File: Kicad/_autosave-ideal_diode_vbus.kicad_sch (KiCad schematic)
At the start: 20 parts, among them J2 USB_B_Micro, Q3 AON7422G, Q4 AON7422G, U5 LD1117S33TR_SOT223, U6 LM74700QDBVRQ1, U7 LM74700QDBVTQ1

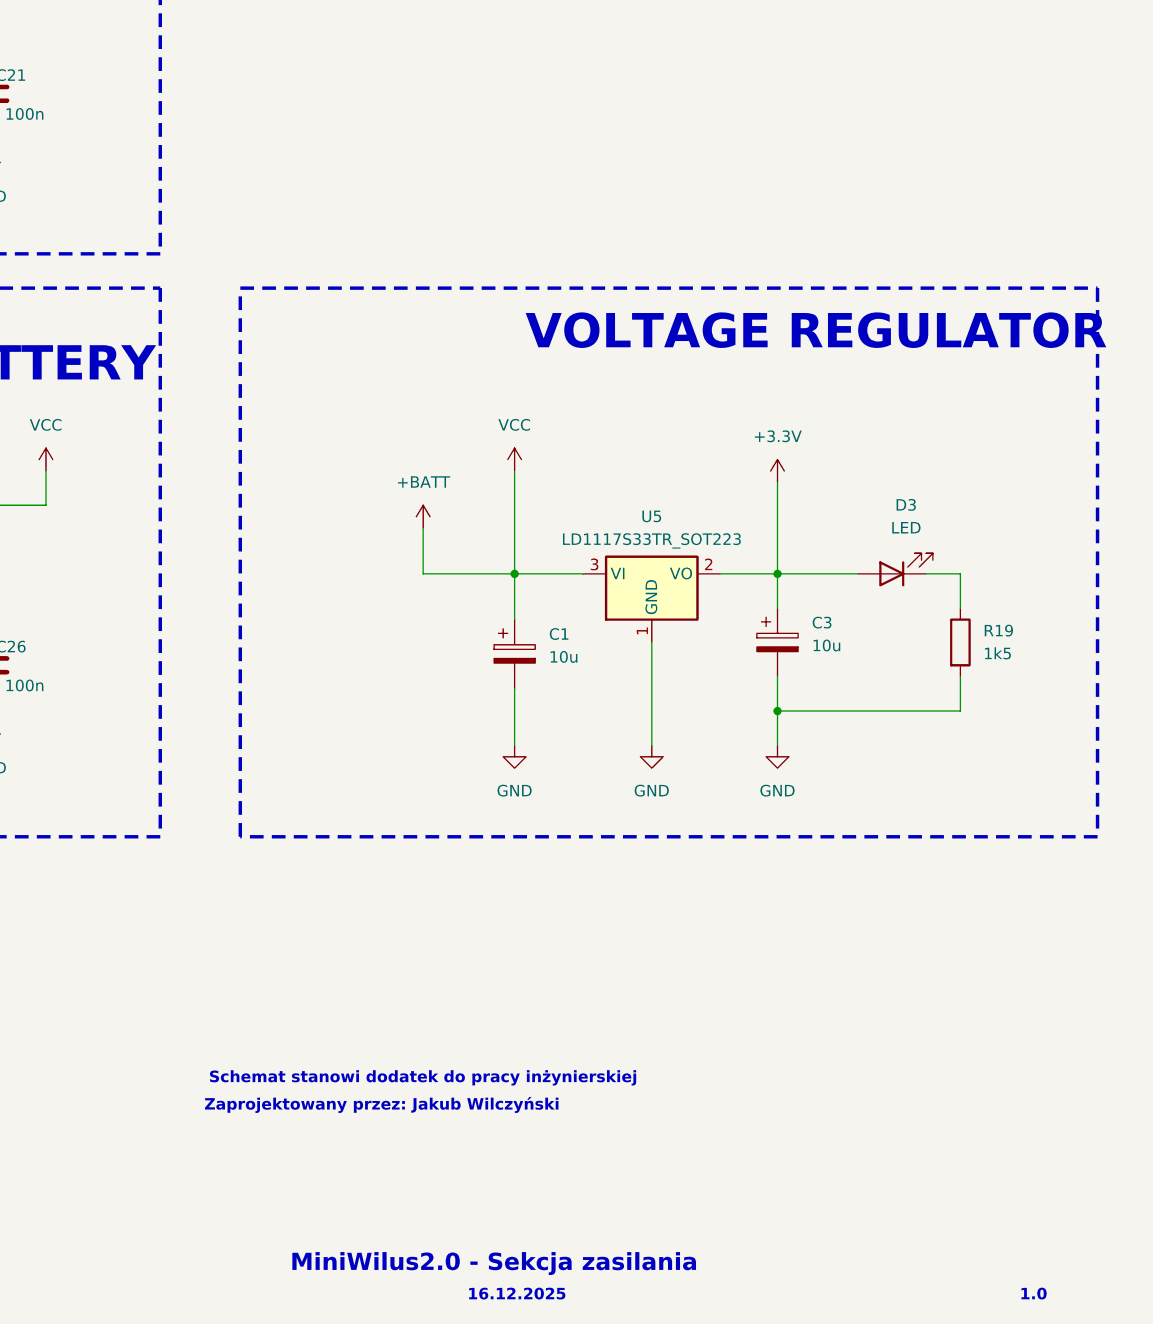
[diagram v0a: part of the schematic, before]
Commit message: kicad schemas documentation
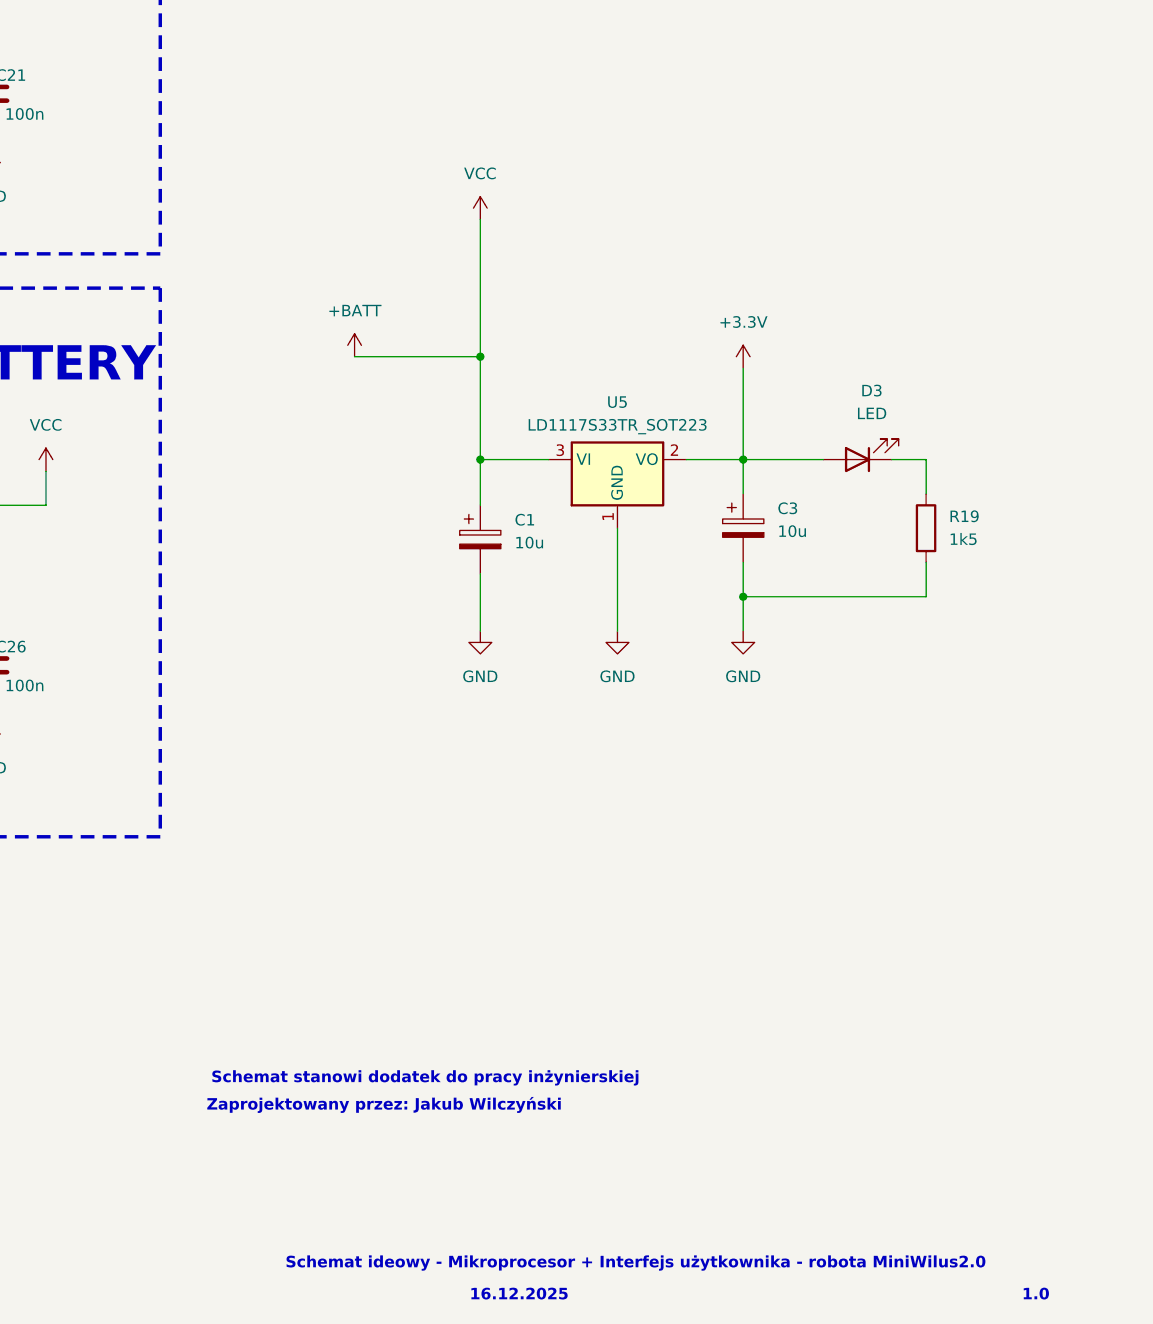
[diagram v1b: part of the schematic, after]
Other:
- note added: "Schemat ideowy - Mikroprocesor + Interfejs użytkownika - robota MiniWilus2.0"
- note removed: "MiniWilus2.0 - Sekcja zasilania"
- note removed: "VOLTAGE REGULATOR"
- moved on the sheet: C1, C3, D3, R19, U5
